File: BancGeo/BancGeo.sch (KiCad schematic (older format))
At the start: 102 parts

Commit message: Update layout
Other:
- moved on the sheet: P?
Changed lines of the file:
@@
 LIBS:contrib
 LIBS:valves
-LIBS:IDBox
 LIBS:BancGeo-cache
+LIBS:YameLib
 EELAYER 25 0
 EELAYER END
@@
 L CONN_01X05 P?
 U 1 1 56BBEC48
-P 6050 1100
-F 0 "P?" H 6050 1400 50  0000 C CNN
-F 1 "CONN_01X05" V 6150 1100 50  0000 C CNN
-F 2 "" H 6050 1100 60  0000 C CNN
-F 3 "" H 6050 1100 60  0000 C CNN
-	1    6050 1100
+P 5750 1100
+F 0 "P?" H 5750 1400 50  0000 C CNN
+F 1 "CONN_01X05" V 5850 1100 50  0000 C CNN
+F 2 "" H 5750 1100 60  0000 C CNN
+F 3 "" H 5750 1100 60  0000 C CNN
+	1    5750 1100
 	-1   0    0    -1
 $EndComp
-Text Label 6350 900  0    60   ~ 0
+Text Label 6050 1100 0    60   ~ 0
 +5V
 $Comp
@@
 	5750 2150 6150 2150
 Wire Wire Line
-	6250 900  6550 900
-Wire Wire Line
-	6250 1300 6300 1300
+	5950 1100 6250 1100
+Wire Wire Line
+	5950 1300 6300 1300
 Wire Wire Line
 	6300 1300 6300 1350
 Wire Wire Line
-	6250 1000 6900 1000
-Wire Wire Line
-	6900 1000 6900 2150
+	6900 900  6900 2150
 Connection ~ 6900 2150
 Wire Wire Line
 	6450 2350 6950 2350
 Wire Wire Line
-	6800 2350 6800 1100
-Wire Wire Line
-	6800 1100 6250 1100
-Wire Wire Line
-	6250 1200 6750 1200
+	6800 1000 6800 2350
 Wire Wire Line
 	6750 1200 6750 2750
@@
 	12550 9300 12550 9250
 Connection ~ 12550 9250
+Wire Wire Line
+	5950 1200 6750 1200
+Wire Wire Line
+	6800 1000 5950 1000
+Wire Wire Line
+	5950 900  6900 900
 $EndSCHEMATC

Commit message: Update BancGeo
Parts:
- T?: value Coupled_Inductor -> DRQ127-100-R
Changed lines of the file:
@@
 P 6100 6850
 F 0 "T?" H 6100 7100 50  0000 C CNN
-F 1 "Coupled_Inductor" H 6100 6550 50  0000 C CNN
+F 1 "DRQ127-100-R" H 6100 6550 50  0000 C CNN
 F 2 "" H 6100 6850 60  0000 C CNN
 F 3 "" H 6100 6850 60  0000 C CNN

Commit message: Update bancgeo
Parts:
- C12, C13, C15, C17, C23, C24, C25, C26, C27, C29, C30, C31, C32, C33, C4, C5, C7, C9: renamed from C?; footprint (none) -> Yame_library:SM0805-MR
- D1: renamed from D?; footprint (none) -> Yame_library:SOT23-MR
- R16, R17: renamed from R?; footprint (none) -> Yame_library:SM0603-MR
- U4: renamed from U?; footprint (none) -> TO_SOT_Packages_SMD:SOT-23-5
- U5: renamed from U?; footprint (none) -> Yame_library:SOT23-MR
- U8: renamed from U?; footprint (none) -> Housings_SSOP:TSSOP-10_3x3mm_Pitch0.5mm
- gave numbers to parts that had none: 78

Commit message: update BancGeo
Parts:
- C1, C10, C11, C14, C18, C19, C2, C20, C21, C28, C3, C6, C8, D3, D4, D5, D6, D7, D8, D9, R1, R10, R11, R12, R13, R14, R15, R18, R19, R2, R20, R21, R22, R23, R24, R25, R26, R27, R28, R29, R3, R30, R31, R32, R33, R34, R4, R5, R6, R7, R8, R9: footprint (none) -> Yame_library:SM0603-MR
- C16, C22: footprint (none) -> Yame_library:SM0805-MR
- P1, P2: footprint (none) -> Connect:PINHEAD1-2
- P3: footprint (none) -> Connect:bornier5
- P4, P5, P6, P7: footprint (none) -> Connect:PINHEAD1-3
- Q1, Q2, Q3, Q4, Q5, U10, U2: footprint (none) -> Yame_library:SOT23-MR
- U1: footprint (none) -> TO_SOT_Packages_THT:TO-92_Inline_Narrow_Oval
- U3: footprint (none) -> Yame_library:SOT23-5-MR
- U6, U9: footprint (none) -> Housings_DFN_QFN:QFN-20-1EP_4x4mm_Pitch0.5mm
- U7: footprint (none) -> Housings_DFN_QFN:QFN-16-1EP_4x4mm_Pitch0.65mm

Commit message: Update Bancgeo
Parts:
- added P8: USB_D-, Yame_library:Test_SMT, symbol CONN_01X01
- added P9: USB_D+, Yame_library:Test_SMT, symbol CONN_01X01
- D2: footprint (none) -> Yame_library:DO-214AC
- SW1: footprint (none) -> Yame_library:Switch_EVQP0
- SW2: footprint (none) -> Yame_library:SW_BancGeo
- T1: footprint (none) -> Yame_library:DRQ127_CPL_TR
- U11: footprint (none) -> Yame_library:HM-10_BLE
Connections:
- wire segments 349 -> 355
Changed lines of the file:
@@
 F 0 "T1" H 6100 7100 50  0000 C CNN
 F 1 "DRQ127-100-R" H 6100 6550 50  0000 C CNN
-F 2 "" H 6100 6850 60  0001 C CNN
+F 2 "Yame_library:DRQ127_CPL_TR" H 6100 6850 60  0001 C CNN
 F 3 "" H 6100 6850 60  0000 C CNN
 	1    6100 6850
@@
 F 0 "D2" H 7200 7150 50  0000 C CNN
 F 1 "SSA33L-E3" H 7200 6950 50  0000 C CNN
-F 2 "" H 7200 7050 60  0001 C CNN
+F 2 "Yame_library:DO-214AC" H 7200 7050 60  0001 C CNN
 F 3 "" H 7200 7050 60  0000 C CNN
 	1    7200 7050
@@
 F 3 "" H 15800 2100 60  0000 C CNN
 	1    15800 2100
-	1    0    0    -1
-$EndComp
-$Comp
-L Switch_DPST SW1
-U 1 1 56BB0B9D
-P 10200 1350
-F 0 "SW1" H 10500 1400 50  0000 C CNN
-F 1 "Switch_DPST" H 10500 1300 50  0000 C CNN
-F 2 "" H 10200 1350 60  0001 C CNN
-F 3 "" H 10200 1350 60  0000 C CNN
-	1    10200 1350
 	1    0    0    -1
 $EndComp
@@
 F 0 "U11" H 13900 6550 60  0000 C CNN
 F 1 "HM-10_BLE_Module" H 14850 6550 60  0000 C CNN
-F 2 "" H 14400 5700 60  0001 C CNN
+F 2 "Yame_library:HM-10_BLE" H 14400 5700 60  0001 C CNN
 F 3 "" H 14400 5700 60  0000 C CNN
 	1    14300 5700
@@
 Connection ~ 9400 1150
 Wire Wire Line
-	9900 1550 9750 1550
-Wire Wire Line
-	9750 1550 9750 1150
-Connection ~ 9750 1150
-Wire Wire Line
 	10500 1150 10850 1150
 Wire Wire Line
 	10850 1150 10850 1650
-Wire Wire Line
-	10500 1550 10850 1550
-Connection ~ 10850 1550
 Wire Wire Line
 	800  6650 950  6650
@@
 F 0 "SW2" H 15550 6310 50  0000 C CNN
 F 1 "SW_PUSH" H 15400 6120 50  0000 C CNN
-F 2 "" H 15400 6200 60  0001 C CNN
+F 2 "Yame_library:SW_BancGeo" H 15400 6200 60  0001 C CNN
 F 3 "" H 15400 6200 60  0000 C CNN
 	1    15400 6200
@@
 Wire Wire Line
 	5950 900  6900 900
+Wire Wire Line
+	9900 1550 9750 1550
+Wire Wire Line
+	9750 1550 9750 1150
+Connection ~ 9750 1150
+Connection ~ 10850 1550
+Wire Wire Line
+	10500 1550 10850 1550
+$Comp
+L Switch_DPST SW1
+U 1 1 56BB0B9D
+P 10200 1350
+F 0 "SW1" H 10500 1400 50  0000 C CNN
+F 1 "Switch_DPST" H 10500 1300 50  0000 C CNN
+F 2 "Yame_library:Switch_EVQP0" H 10200 1350 60  0001 C CNN
+F 3 "" H 10200 1350 60  0000 C CNN
+	1    10200 1350
+	1    0    0    -1
+$EndComp
+$Comp
+L CONN_01X01 P8
+U 1 1 57083033
+P 15050 4400
+F 0 "P8" H 15050 4500 50  0000 C CNN
+F 1 "USB_D-" V 15150 4400 50  0000 C CNN
+F 2 "Yame_library:Test_SMT" H 15050 4400 50  0001 C CNN
+F 3 "" H 15050 4400 50  0000 C CNN
+	1    15050 4400
+	0    -1   -1   0
+$EndComp
+$Comp
+L CONN_01X01 P9
+U 1 1 57083364
+P 15400 4500
+F 0 "P9" H 15400 4600 50  0000 C CNN
+F 1 "USB_D+" V 15500 4500 50  0000 C CNN
+F 2 "Yame_library:Test_SMT" H 15400 4500 50  0001 C CNN
+F 3 "" H 15400 4500 50  0000 C CNN
+	1    15400 4500
+	0    -1   -1   0
+$EndComp
+Wire Wire Line
+	15050 4600 15050 5250
+Wire Wire Line
+	15050 5250 15000 5250
+Wire Wire Line
+	15400 4700 15400 5200
+Wire Wire Line
+	15400 5200 15200 5200
+Wire Wire Line
+	15200 5200 15200 5450
+Wire Wire Line
+	15200 5450 15000 5450
 $EndSCHEMATC

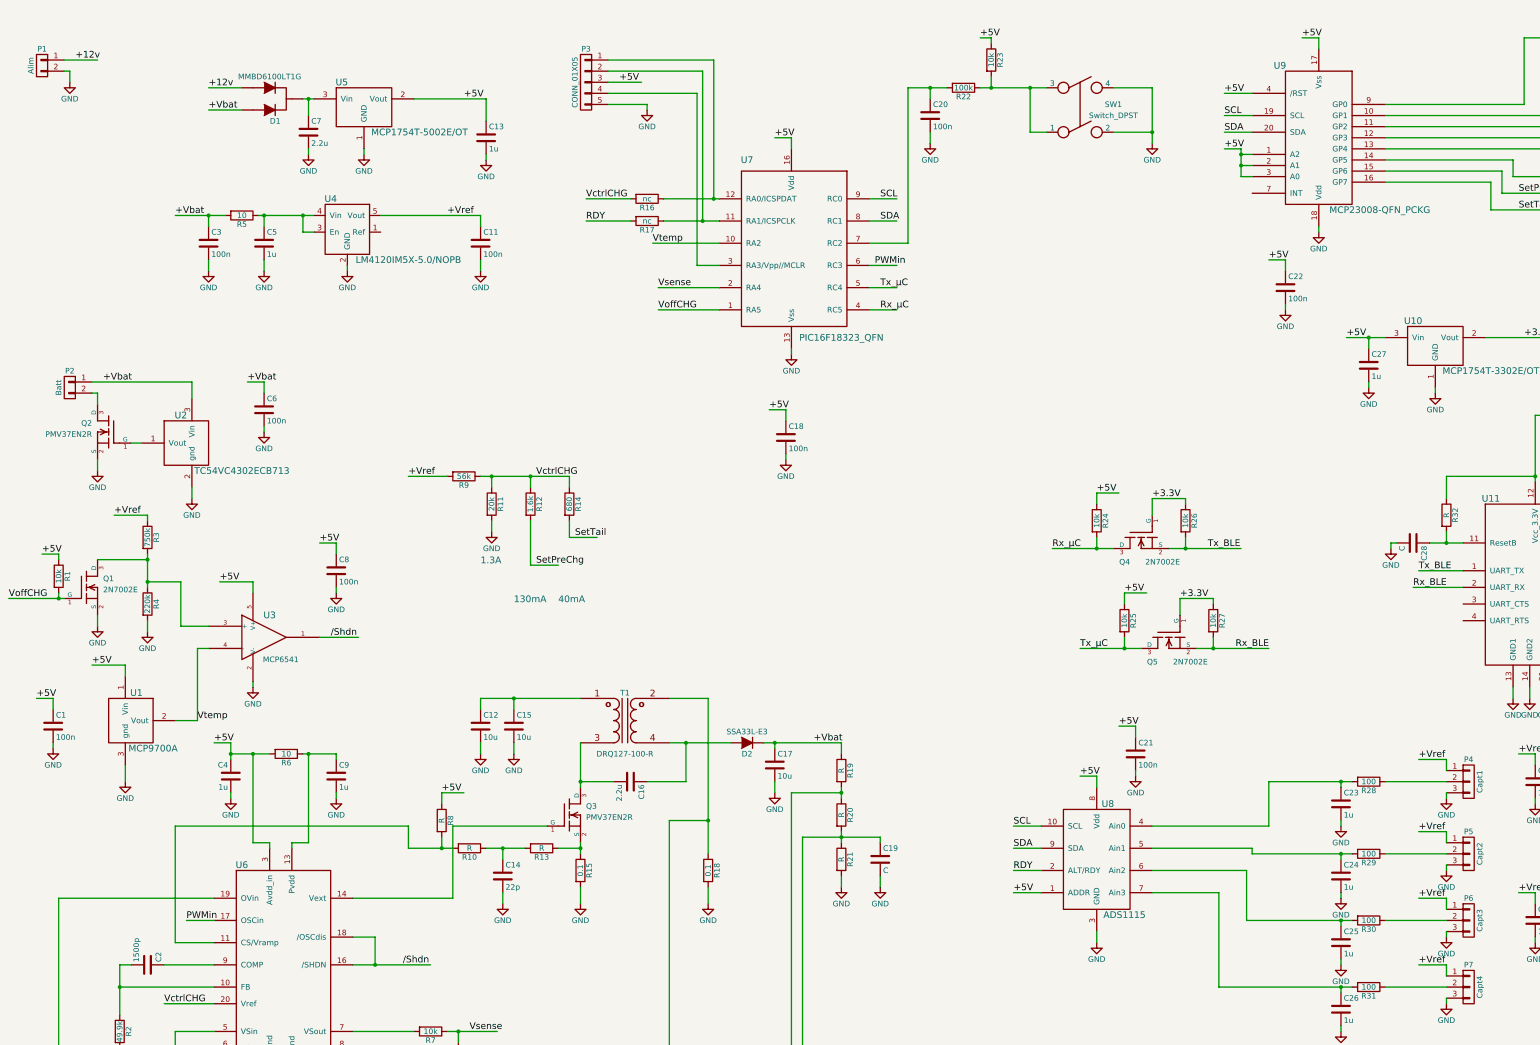
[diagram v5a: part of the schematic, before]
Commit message: update bancgeo
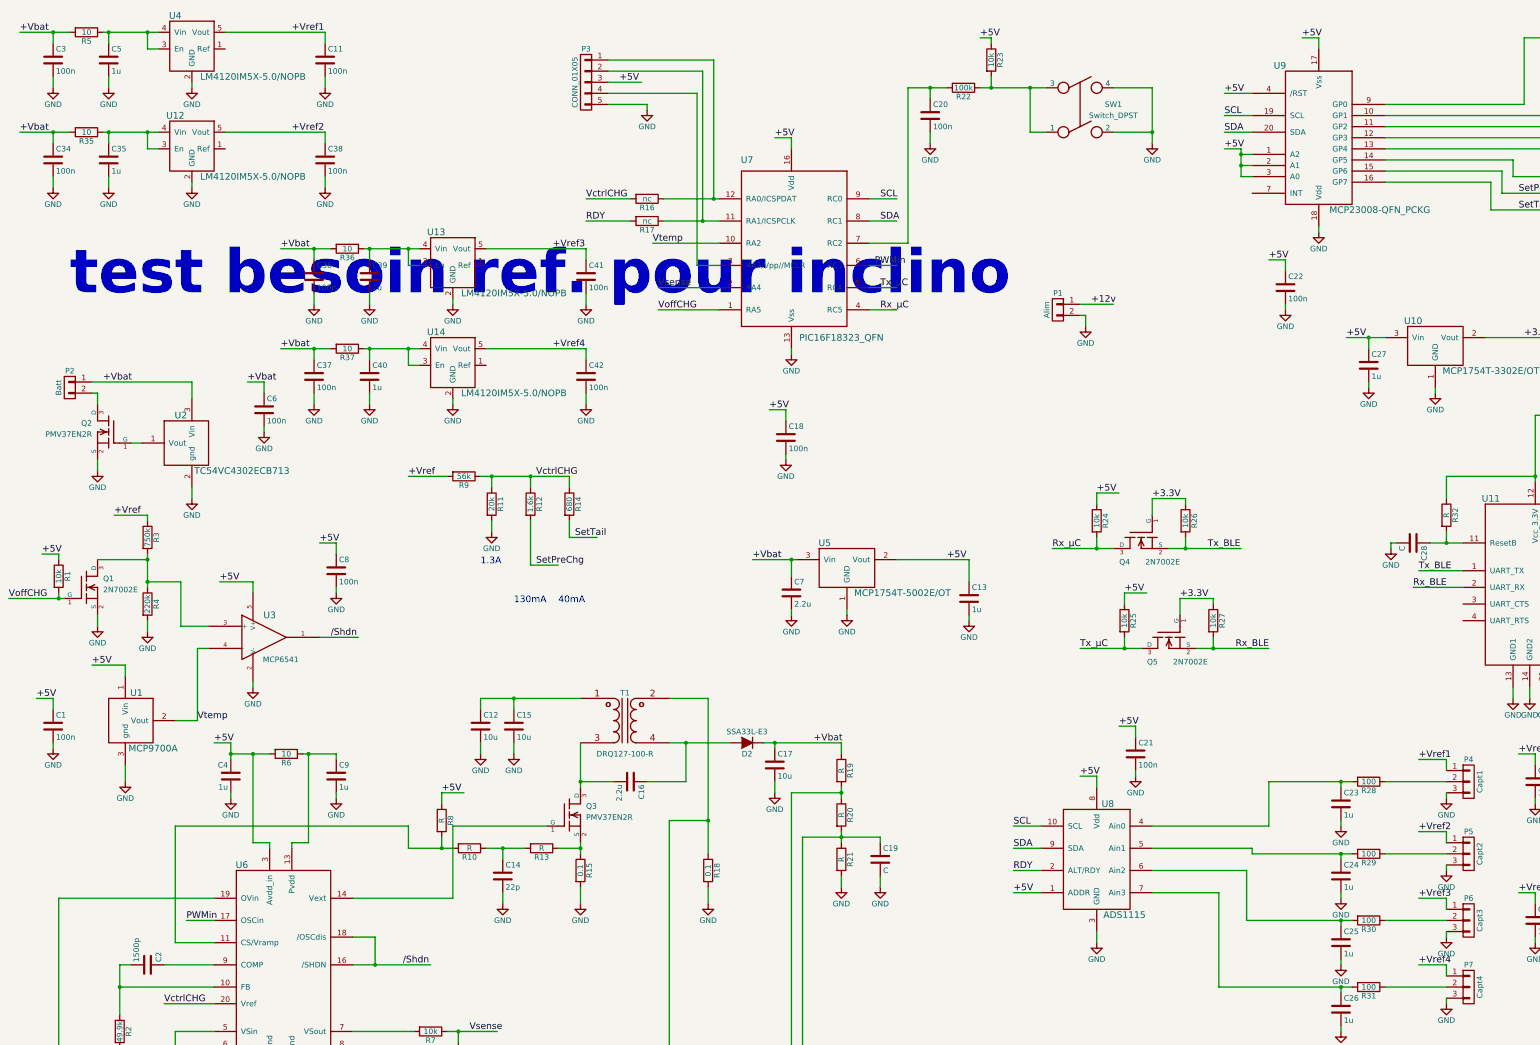
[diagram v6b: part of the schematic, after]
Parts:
- removed D1: MMBD6100LT1G, Yame_library:SOT23-MR, symbol MMBD6100LT1G
- added C34, C36, C37, C38, C41, C42: 100n, Yame_library:SM0603-MR, symbol C
- added C35, C39, C40: 1u, Yame_library:SM0805-MR, symbol C
- added R35, R36, R37: 10, Yame_library:SM0603-MR, symbol R
- added U12, U13, U14: LM4120IM5X-5.0/NOPB, TO_SOT_Packages_SMD:SOT-23-5, symbol LM4120
- D3, D4, D5, D7, D8, D9: footprint Yame_library:SM0603-MR -> LEDs:LED-5MM
- D6: footprint Yame_library:SM0603-MR -> LEDs:LED_0603
- P3: footprint Connect:bornier5 -> Yame_library:HE10_14-5C-2.54-MR
- P8, P9: footprint Yame_library:Test_SMT -> Yame_library:Test_Point_T_H
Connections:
- net labels added: +Vref1, +Vref2, +Vref3, +Vref4
- wire segments 355 -> 389
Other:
- note added: "test besoin ref. pour inclino"
- moved on the sheet: C11, C13, C3, C5, C7, P1, R5, U4, U5

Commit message: Update BancGeo
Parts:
- removed SW1: Switch_DPST, Yame_library:Switch_EVQP0, symbol Switch_DPST
- added R38, R39, R40, R41, R42, R43: 470, Yame_library:SM0603-MR, symbol R
- added SW1: SWITCH_BRIDE, SWITCH_BRIDE, symbol SWITCH_BRIDE
- SW2: footprint Yame_library:SW_BancGeo -> Buttons_Switches_SMD:SW_SPST_B3U-1000P
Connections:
- wire segments 389 -> 398
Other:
- note removed: "test besoin ref. pour inclino"

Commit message: Update Bancgeo
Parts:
- removed C36, C37, C41, C42: 100n, Yame_library:SM0603-MR, symbol C
- removed C39, C40: 1u, Yame_library:SM0805-MR, symbol C
- removed R36, R37: 10, Yame_library:SM0603-MR, symbol R
- removed U13, U14: LM4120IM5X-5.0/NOPB, TO_SOT_Packages_SMD:SOT-23-5, symbol LM4120
- U1: footprint TO_SOT_Packages_THT:TO-92_Inline_Narrow_Oval -> Yame_library:SOT23-MR
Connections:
- net labels removed: +Vref, +Vref3, +Vref4
- wire segments 398 -> 374
